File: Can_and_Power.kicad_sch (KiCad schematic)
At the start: 11 parts, among them J4 776280-1, J5 776280-1, U2 ADM3057EBRWZ

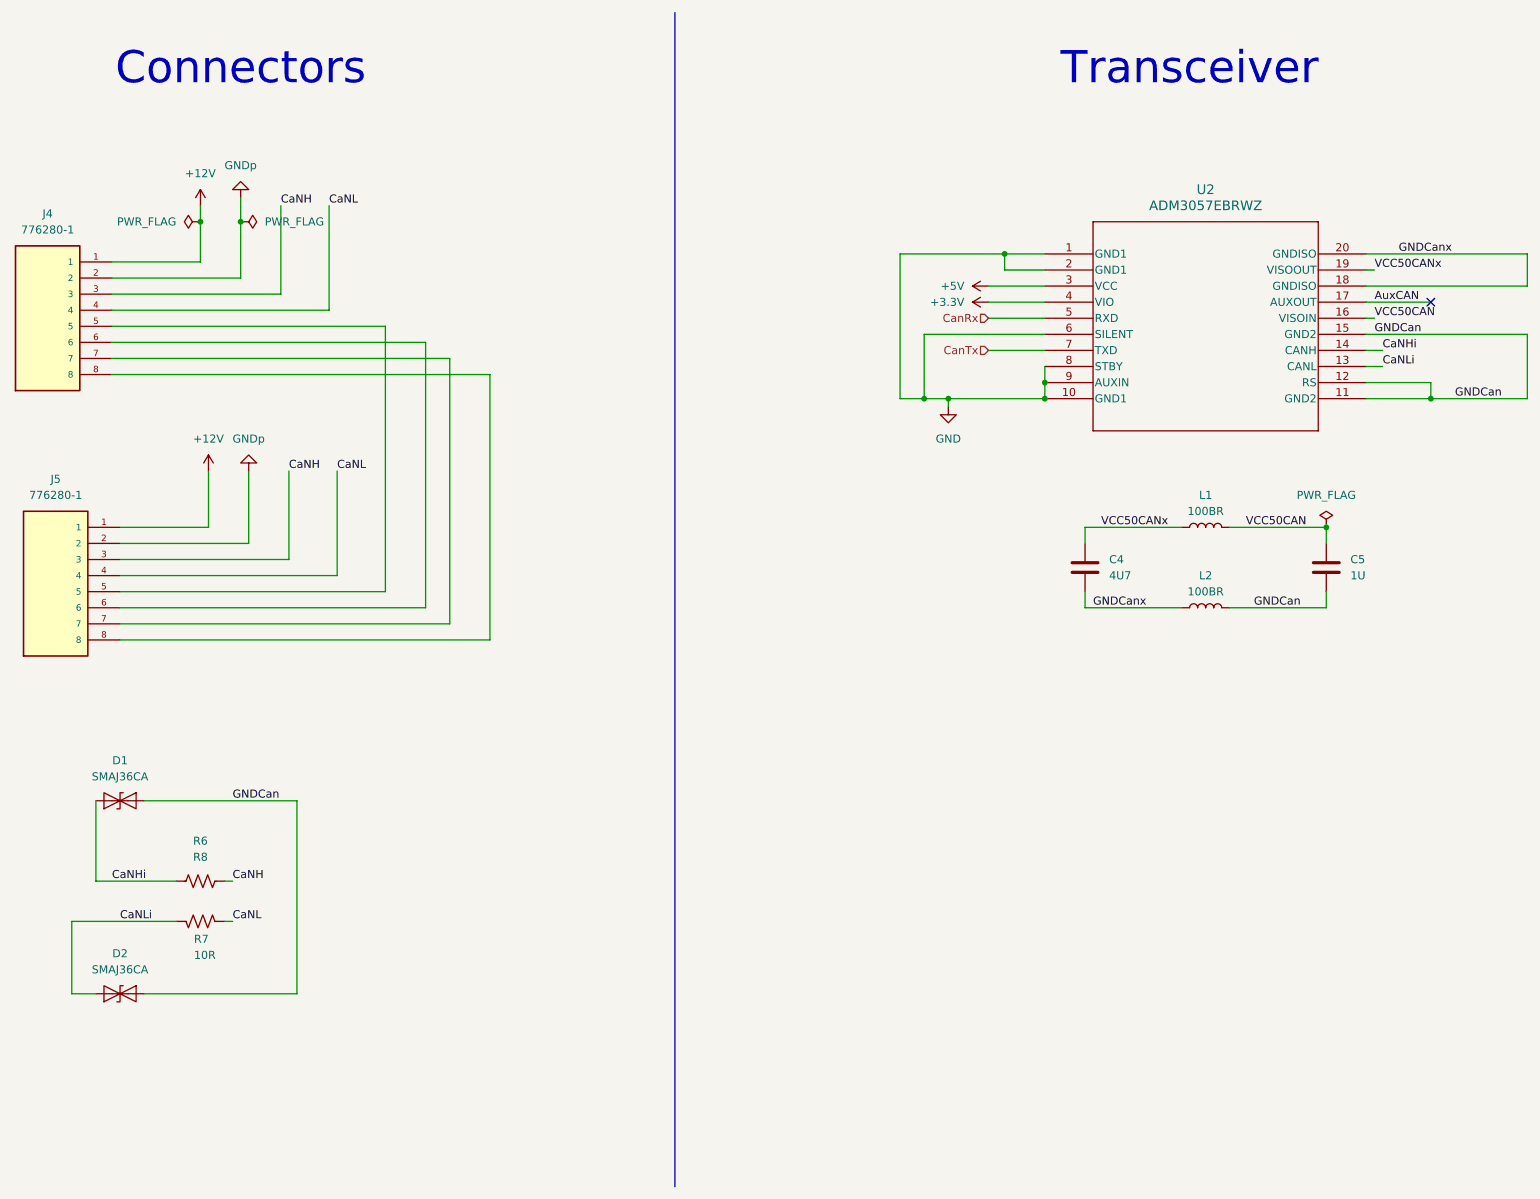
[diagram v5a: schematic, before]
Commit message: made connector match drawing
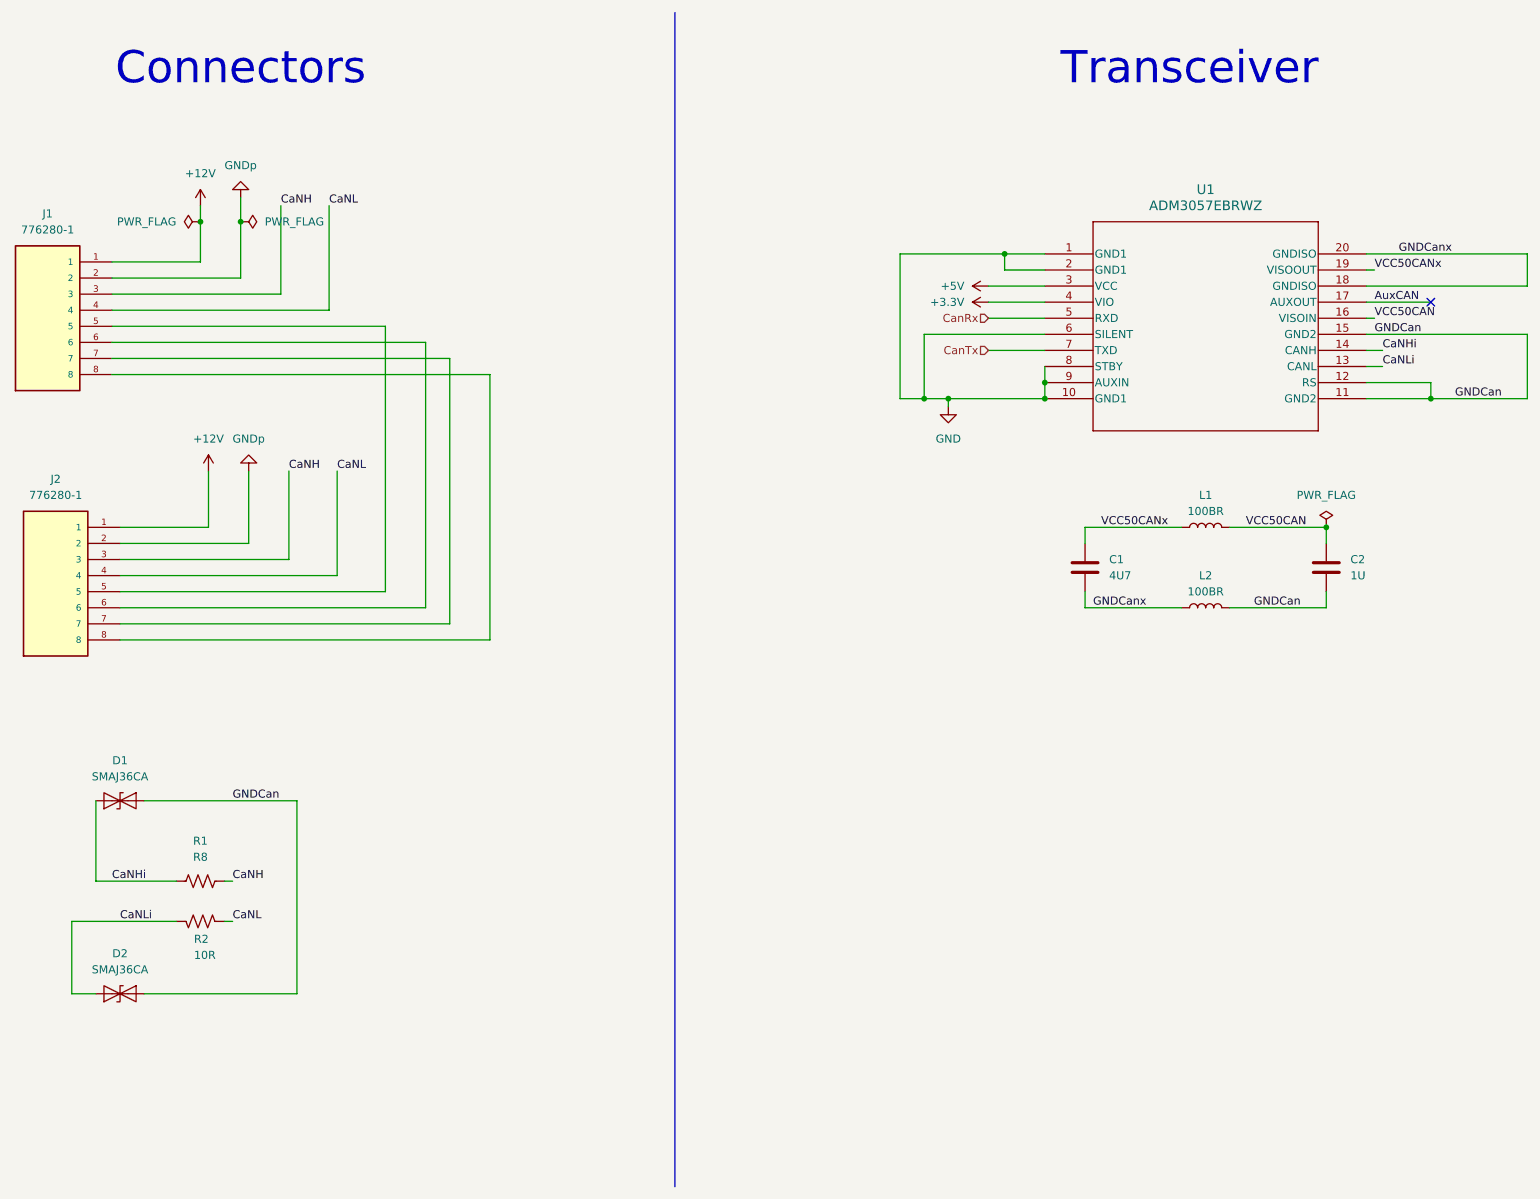
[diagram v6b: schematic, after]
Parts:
- renumbered C4 to C1, C5 to C2, J4 to J1, J5 to J2, R6 to R1, R7 to R2, U2 to U1
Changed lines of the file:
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@@
 		(dnp no)
 		(fields_autoplaced yes)
-		(property "Reference" "#PWR026"
+		(property "Reference" "#PWR07"
 			(at 189.23 58.42 0)
 			(effects
@@
 		(instances
 			(project "Main-Board-V2"
-				(path "/c01682a2-308a-4674-9b8f-80e441c05d08/82598d9f-7302-484e-880f-c9b73897b20c"
-					(reference "#PWR026")
+				(path "/c01682a2-308a-4674-9b8f-80e441c05d08/2eeb5b34-c445-4914-b41b-f611e24c0c64"
+					(reference "#PWR07")
 					(unit 1)
 				)
@@
 		(dnp no)
 		(fields_autoplaced yes)
-		(property "Reference" "#PWR020"
+		(property "Reference" "#PWR01"
 			(at 60.96 46.99 0)
 			(effects
@@
 		(instances
 			(project "Main-Board-V2"
-				(path "/c01682a2-308a-4674-9b8f-80e441c05d08/82598d9f-7302-484e-880f-c9b73897b20c"
-					(reference "#PWR020")
+				(path "/c01682a2-308a-4674-9b8f-80e441c05d08/2eeb5b34-c445-4914-b41b-f611e24c0c64"
+					(reference "#PWR01")
 					(unit 1)
 				)
@@
 		(dnp no)
 		(fields_autoplaced yes)
-		(property "Reference" "#PWR025"
+		(property "Reference" "#PWR06"
 			(at 189.23 55.88 0)
 			(effects
@@
 		(instances
 			(project "Main-Board-V2"
-				(path "/c01682a2-308a-4674-9b8f-80e441c05d08/82598d9f-7302-484e-880f-c9b73897b20c"
-					(reference "#PWR025")
+				(path "/c01682a2-308a-4674-9b8f-80e441c05d08/2eeb5b34-c445-4914-b41b-f611e24c0c64"
+					(reference "#PWR06")
 					(unit 1)
 				)
@@
 		(dnp no)
 		(fields_autoplaced yes)
-		(property "Reference" "#FLG03"
+		(property "Reference" "#FLG02"
 			(at 69.215 45.72 0)
 			(effects
@@
 		(instances
 			(project "Main-Board-V2"
-				(path "/c01682a2-308a-4674-9b8f-80e441c05d08/82598d9f-7302-484e-880f-c9b73897b20c"
-					(reference "#FLG03")
+				(path "/c01682a2-308a-4674-9b8f-80e441c05d08/2eeb5b34-c445-4914-b41b-f611e24c0c64"
+					(reference "#FLG02")
 					(unit 1)
 				)
@@
 		(on_board yes)
 		(dnp no)
-		(property "Reference" "J4"
+		(property "Reference" "J1"
 			(at 36.83 44.45 0)
 			(effects
@@
 		(instances
 			(project "Main-Board-V2"
-				(path "/c01682a2-308a-4674-9b8f-80e441c05d08/82598d9f-7302-484e-880f-c9b73897b20c"
-					(reference "J4")
+				(path "/c01682a2-308a-4674-9b8f-80e441c05d08/2eeb5b34-c445-4914-b41b-f611e24c0c64"
+					(reference "J1")
 					(unit 1)
 				)
@@
 		(dnp no)
 		(fields_autoplaced yes)
-		(property "Reference" "C5"
+		(property "Reference" "C2"
 			(at 242.57 99.0599 0)
 			(effects
@@
 		(instances
 			(project "Main-Board-V2"
-				(path "/c01682a2-308a-4674-9b8f-80e441c05d08/82598d9f-7302-484e-880f-c9b73897b20c"
-					(reference "C5")
+				(path "/c01682a2-308a-4674-9b8f-80e441c05d08/2eeb5b34-c445-4914-b41b-f611e24c0c64"
+					(reference "C2")
 					(unit 1)
 				)
@@
 		(dnp no)
 		(fields_autoplaced yes)
-		(property "Reference" "#FLG04"
+		(property "Reference" "#FLG03"
 			(at 238.76 92.075 0)
 			(effects
@@
 		(instances
 			(project "Main-Board-V2"
-				(path "/c01682a2-308a-4674-9b8f-80e441c05d08/82598d9f-7302-484e-880f-c9b73897b20c"
-					(reference "#FLG04")
+				(path "/c01682a2-308a-4674-9b8f-80e441c05d08/2eeb5b34-c445-4914-b41b-f611e24c0c64"
+					(reference "#FLG03")
 					(unit 1)
 				)
@@
 		(dnp no)
 		(fields_autoplaced yes)
-		(property "Reference" "R6"
+		(property "Reference" "R1"
 			(at 60.96 143.51 90)
 			(effects
@@
 		(instances
 			(project "Main-Board-V2"
-				(path "/c01682a2-308a-4674-9b8f-80e441c05d08/82598d9f-7302-484e-880f-c9b73897b20c"
-					(reference "R6")
+				(path "/c01682a2-308a-4674-9b8f-80e441c05d08/2eeb5b34-c445-4914-b41b-f611e24c0c64"
+					(reference "R1")
 					(unit 1)
 				)
@@
 		(instances
 			(project "Main-Board-V2"
-				(path "/c01682a2-308a-4674-9b8f-80e441c05d08/82598d9f-7302-484e-880f-c9b73897b20c"
+				(path "/c01682a2-308a-4674-9b8f-80e441c05d08/2eeb5b34-c445-4914-b41b-f611e24c0c64"
 					(reference "D2")
 					(unit 1)
@@
 		(dnp no)
 		(fields_autoplaced yes)
-		(property "Reference" "#FLG02"
+		(property "Reference" "#FLG01"
 			(at 59.055 45.72 0)
 			(effects
@@
 		(instances
 			(project "Main-Board-V2"
-				(path "/c01682a2-308a-4674-9b8f-80e441c05d08/82598d9f-7302-484e-880f-c9b73897b20c"
-					(reference "#FLG02")
+				(path "/c01682a2-308a-4674-9b8f-80e441c05d08/2eeb5b34-c445-4914-b41b-f611e24c0c64"
+					(reference "#FLG01")
 					(unit 1)
 				)
@@
 		(dnp no)
 		(fields_autoplaced yes)
-		(property "Reference" "#PWR022"
+		(property "Reference" "#PWR03"
 			(at 67.31 35.56 0)
 			(effects
@@
 		(instances
 			(project "Main-Board-V2"
-				(path "/c01682a2-308a-4674-9b8f-80e441c05d08/82598d9f-7302-484e-880f-c9b73897b20c"
-					(reference "#PWR022")
+				(path "/c01682a2-308a-4674-9b8f-80e441c05d08/2eeb5b34-c445-4914-b41b-f611e24c0c64"
+					(reference "#PWR03")
 					(unit 1)
 				)
@@
 		(on_board yes)
 		(dnp no)
-		(property "Reference" "J5"
+		(property "Reference" "J2"
 			(at 38.1 86.36 0)
 			(effects
@@
 		(instances
 			(project "Main-Board-V2"
-				(path "/c01682a2-308a-4674-9b8f-80e441c05d08/82598d9f-7302-484e-880f-c9b73897b20c"
-					(reference "J5")
+				(path "/c01682a2-308a-4674-9b8f-80e441c05d08/2eeb5b34-c445-4914-b41b-f611e24c0c64"
+					(reference "J2")
 					(unit 1)
 				)
@@
 		(dnp no)
 		(fields_autoplaced yes)
-		(property "Reference" "U2"
+		(property "Reference" "U1"
 			(at 219.71 40.64 0)
 			(effects
@@
 		(instances
 			(project "Main-Board-V2"
-				(path "/c01682a2-308a-4674-9b8f-80e441c05d08/82598d9f-7302-484e-880f-c9b73897b20c"
-					(reference "U2")
+				(path "/c01682a2-308a-4674-9b8f-80e441c05d08/2eeb5b34-c445-4914-b41b-f611e24c0c64"
+					(reference "U1")
 					(unit 1)
 				)
@@
 		(on_board yes)
 		(dnp no)
-		(property "Reference" "R7"
+		(property "Reference" "R2"
 			(at 59.944 159.004 90)
 			(effects
@@
 		(instances
 			(project "Main-Board-V2"
-				(path "/c01682a2-308a-4674-9b8f-80e441c05d08/82598d9f-7302-484e-880f-c9b73897b20c"
-					(reference "R7")
+				(path "/c01682a2-308a-4674-9b8f-80e441c05d08/2eeb5b34-c445-4914-b41b-f611e24c0c64"
+					(reference "R2")
 					(unit 1)
 				)
@@
 		(dnp no)
 		(fields_autoplaced yes)
-		(property "Reference" "#PWR021"
+		(property "Reference" "#PWR02"
 			(at 62.23 88.9 0)
 			(effects
@@
 		(instances
 			(project "Main-Board-V2"
-				(path "/c01682a2-308a-4674-9b8f-80e441c05d08/82598d9f-7302-484e-880f-c9b73897b20c"
-					(reference "#PWR021")
+				(path "/c01682a2-308a-4674-9b8f-80e441c05d08/2eeb5b34-c445-4914-b41b-f611e24c0c64"
+					(reference "#PWR02")
 					(unit 1)
 				)
@@
 		(dnp no)
 		(fields_autoplaced yes)
-		(property "Reference" "#PWR023"
+		(property "Reference" "#PWR04"
 			(at 68.58 78.74 0)
 			(effects
@@
 		(instances
 			(project "Main-Board-V2"
-				(path "/c01682a2-308a-4674-9b8f-80e441c05d08/82598d9f-7302-484e-880f-c9b73897b20c"
-					(reference "#PWR023")
+				(path "/c01682a2-308a-4674-9b8f-80e441c05d08/2eeb5b34-c445-4914-b41b-f611e24c0c64"
+					(reference "#PWR04")
 					(unit 1)
 				)
@@
 		(dnp no)
 		(fields_autoplaced yes)
-		(property "Reference" "#PWR024"
+		(property "Reference" "#PWR05"
 			(at 179.07 81.28 0)
 			(effects
@@
 		(instances
 			(project "Main-Board-V2"
-				(path "/c01682a2-308a-4674-9b8f-80e441c05d08/82598d9f-7302-484e-880f-c9b73897b20c"
-					(reference "#PWR024")
+				(path "/c01682a2-308a-4674-9b8f-80e441c05d08/2eeb5b34-c445-4914-b41b-f611e24c0c64"
+					(reference "#PWR05")
 					(unit 1)
 				)
@@
 		(instances
 			(project "Main-Board-V2"
-				(path "/c01682a2-308a-4674-9b8f-80e441c05d08/82598d9f-7302-484e-880f-c9b73897b20c"
+				(path "/c01682a2-308a-4674-9b8f-80e441c05d08/2eeb5b34-c445-4914-b41b-f611e24c0c64"
 					(reference "D1")
 					(unit 1)
@@
 		(dnp no)
 		(fields_autoplaced yes)
-		(property "Reference" "C4"
+		(property "Reference" "C1"
 			(at 204.47 99.0599 0)
 			(effects
@@
 		(instances
 			(project "Main-Board-V2"
-				(path "/c01682a2-308a-4674-9b8f-80e441c05d08/82598d9f-7302-484e-880f-c9b73897b20c"
-					(reference "C4")
+				(path "/c01682a2-308a-4674-9b8f-80e441c05d08/2eeb5b34-c445-4914-b41b-f611e24c0c64"
+					(reference "C1")
 					(unit 1)
 				)
@@
 		(instances
 			(project "Main-Board-V2"
-				(path "/c01682a2-308a-4674-9b8f-80e441c05d08/82598d9f-7302-484e-880f-c9b73897b20c"
+				(path "/c01682a2-308a-4674-9b8f-80e441c05d08/2eeb5b34-c445-4914-b41b-f611e24c0c64"
 					(reference "L1")
 					(unit 1)
@@
 		(instances
 			(project "Main-Board-V2"
-				(path "/c01682a2-308a-4674-9b8f-80e441c05d08/82598d9f-7302-484e-880f-c9b73897b20c"
+				(path "/c01682a2-308a-4674-9b8f-80e441c05d08/2eeb5b34-c445-4914-b41b-f611e24c0c64"
 					(reference "L2")
 					(unit 1)
